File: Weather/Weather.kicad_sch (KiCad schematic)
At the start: 48 parts

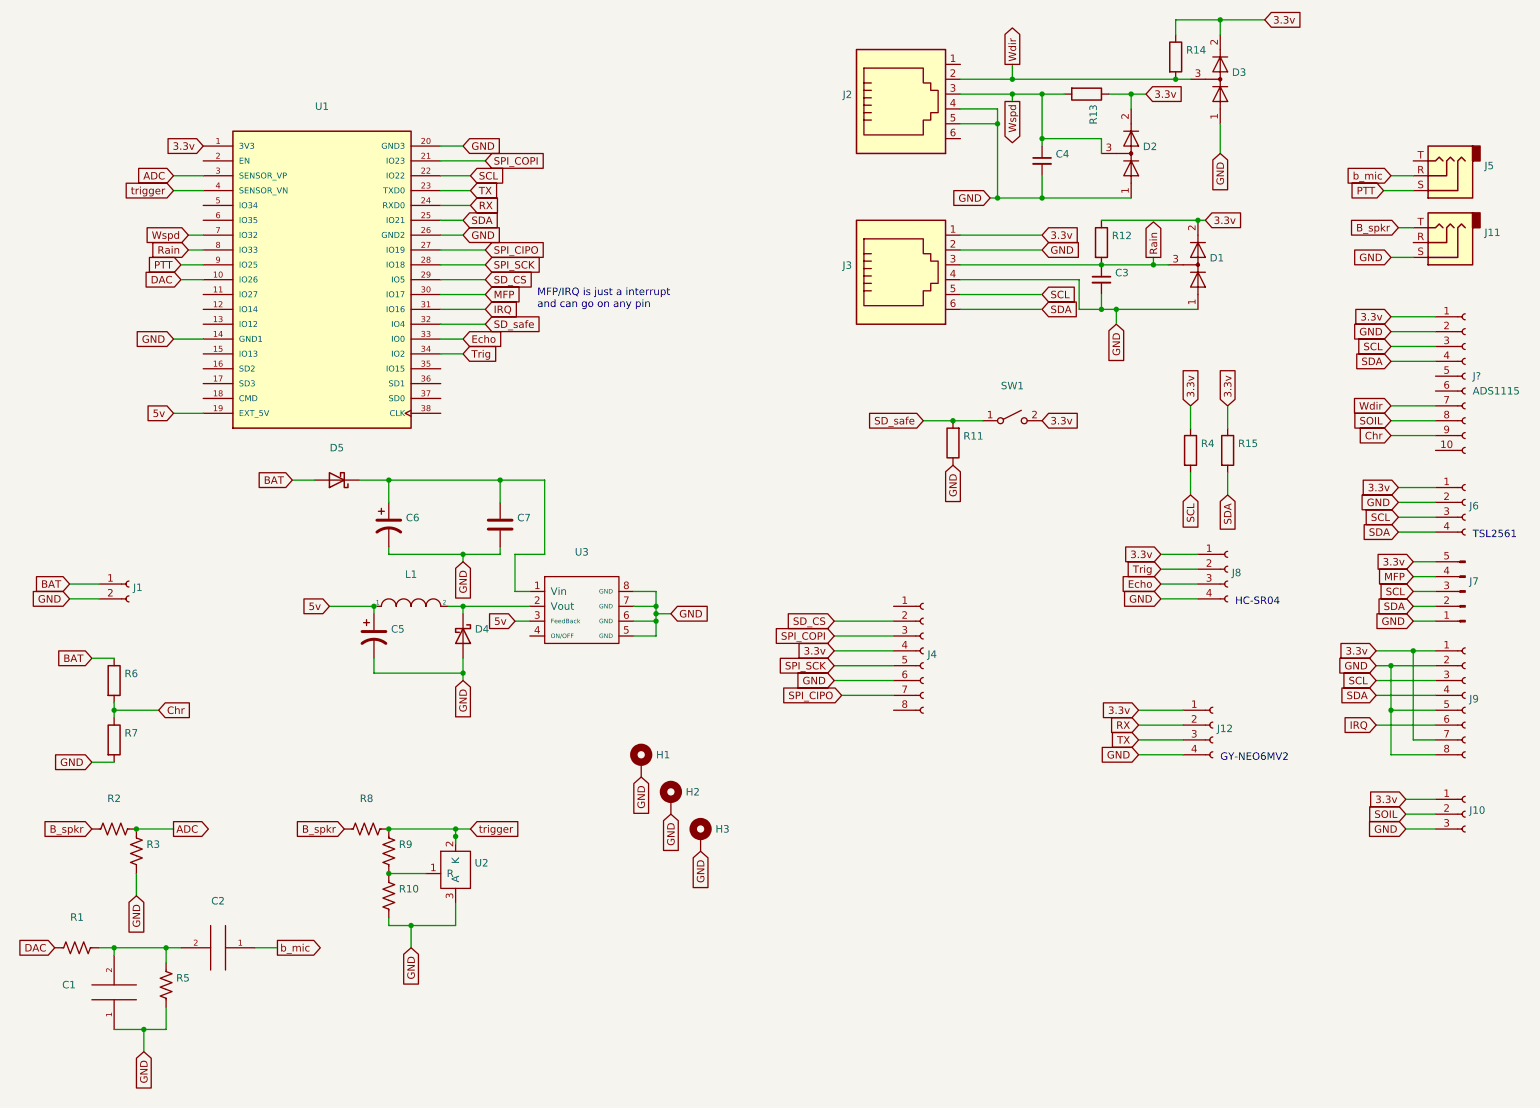
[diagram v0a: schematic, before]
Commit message: Missed some files and corrected a resistor setup
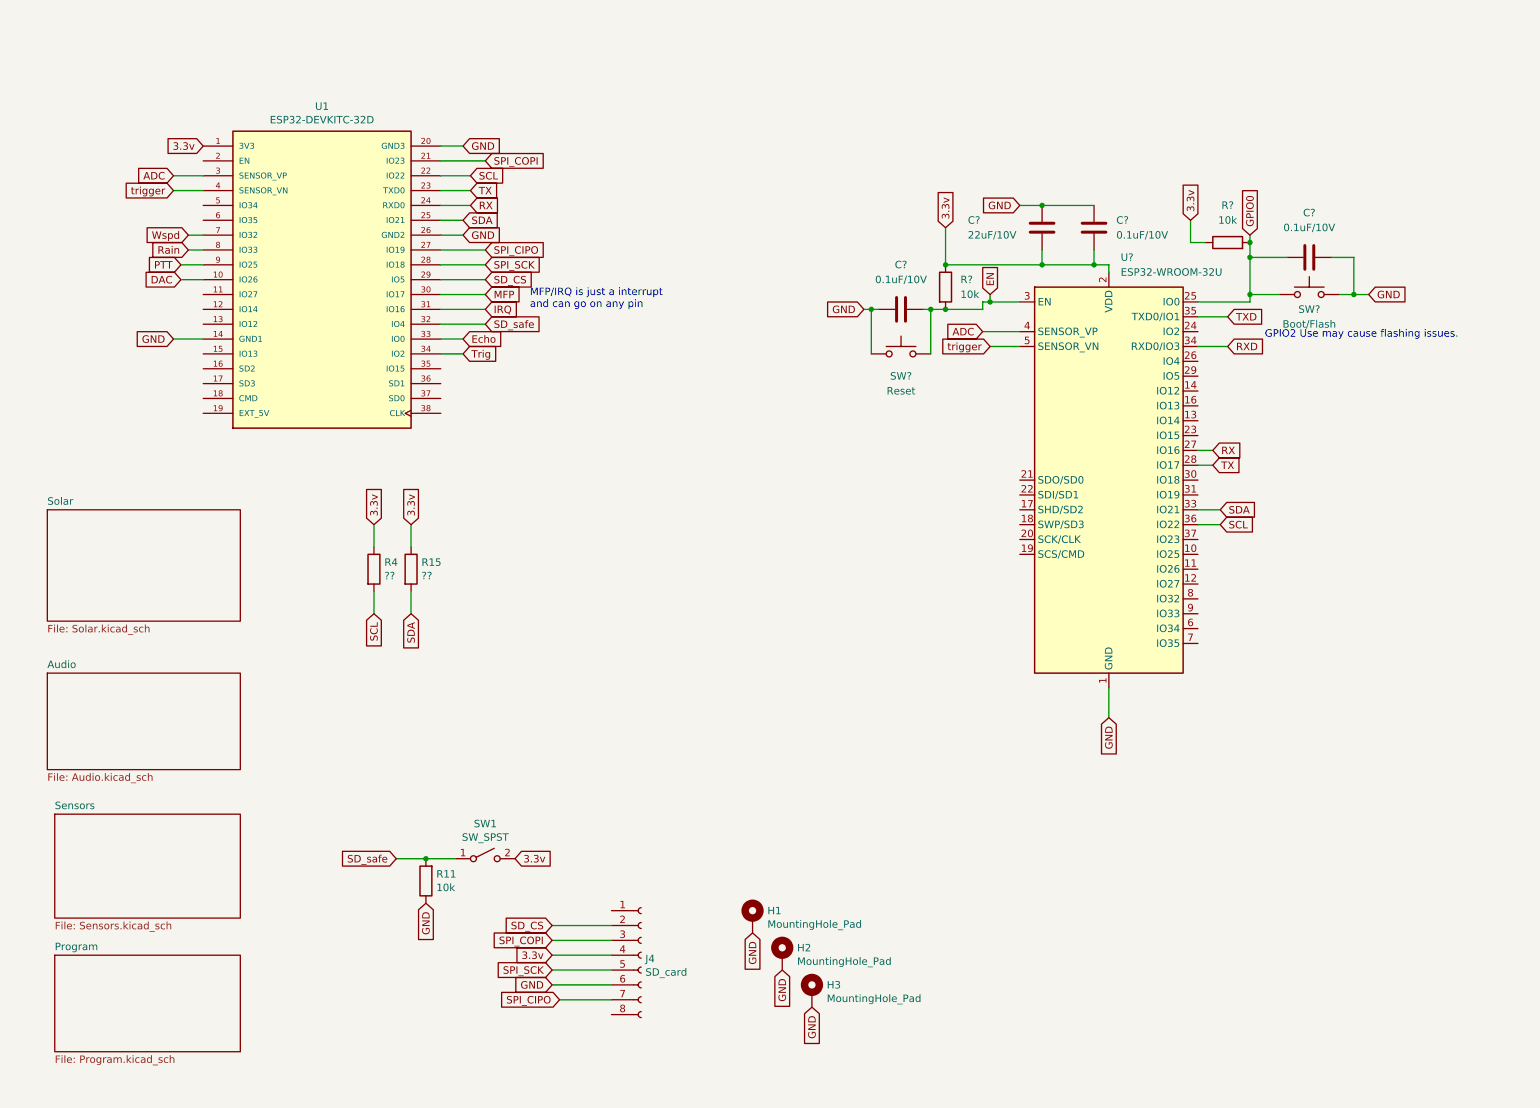
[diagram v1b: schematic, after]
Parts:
- removed C1, C2: (no value), symbol pspice:CAP
- removed C3, C4: (no value), symbol Device:C_Small
- removed C5, C6: (no value), symbol Device:CP1
- removed C7: (no value), symbol Device:C
- removed D1, D2, D3: (no value), symbol Diode:BAV99
- removed D4: (no value), symbol Diode:1N5820
- removed D5: (no value), symbol Diode:1N5819
- removed J1: (no value), symbol Connector:Conn_01x02_Female
- removed J10: (no value), symbol Connector:Conn_01x03_Female
- removed J11, J5: (no value), symbol Connector:AudioJack3
- removed J12, J6, J8: (no value), symbol Connector:Conn_01x04_Female
- removed J2, J3: (no value), symbol Connector:RJ12
- removed J7: (no value), symbol Connector:Conn_01x05_Male
- removed J9: (no value), symbol Connector:Conn_01x08_Female
- removed J?: ADS1115, symbol Connector:Conn_01x10_Female
- removed L1: (no value), symbol pspice:INDUCTOR
- removed R1, R10, R2, R3, R5, R8, R9: (no value), symbol Device:R_US
- removed R12, R13, R14, R6, R7: (no value), symbol Device:R
- removed U2: (no value), symbol Weather-rescue:CJ431
- removed U3: (no value), symbol Darty_stuff:XL1509-5.0E1
- added C? (x3): 0.1uF/10V, symbol Device:C
- added C?: 22uF/10V, symbol Device:C
- added R? (x2): 10k, symbol Device:R
- added SW?: Boot/Flash, symbol Switch:SW_Push
- added SW?: Reset, symbol Switch:SW_Push
- added U?: ESP32-WROOM-32U, RF_Module:ESP32-WROOM-32U, symbol RF_Module:ESP32-WROOM-32U
- H1, H2, H3: value (none) -> MountingHole_Pad; footprint (none) -> MountingHole:MountingHole_3.2mm_M3_Pad_Via
- J4: value (none) -> SD_card; footprint (none) -> Connector_PinSocket_2.54mm:PinSocket_1x08_P2.54mm_Vertical
- R11: value (none) -> 10k; footprint (none) -> Resistor_SMD:R_1206_3216Metric_Pad1.30x1.75mm_HandSolder
- R15, R4: value (none) -> ??; footprint (none) -> Resistor_THT:R_Axial_DIN0207_L6.3mm_D2.5mm_P7.62mm_Horizontal
- SW1: value (none) -> SW_SPST; footprint (none) -> Connector_PinHeader_2.54mm:PinHeader_1x02_P2.54mm_Vertical
- U1: value (none) -> ESP32-DEVKITC-32D; footprint (none) -> ESP32-DEVKITC-32D:MODULE_ESP32-DEVKITC-32D
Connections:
- net 3.3v: now also C?.2, C?.2, R?.1, R?.1, U?.2 (VDD)
- net ADC: now also U?.4 (SENSOR_VP)
- net GND: now also C?.1, C?.1, C?.1, C?.2, SW?.1, SW?.2, U?.1 (GND), U?.15 (GND), U?.38 (GND), U?.39 (GND)
- net RX: now also U?.27 (IO16)
- net SCL: now also U?.36 (IO22)
- net SDA: now also U?.33 (IO21)
- net TX: now also U?.28 (IO17)
- net trigger: now also U?.5 (SENSOR_VN)
- net 5v: no longer names the net of U1.19 (EXT_5V)
- new net EN: C?.1, R?.2, SW?.2, U?.3 (EN)
- new net GPIO0: C?.2, R?.2, SW?.1, U?.25 (IO0)
- new net RXD: U?.34 (RXD0/IO3)
- new net TXD: U?.35 (TXD0/IO1)
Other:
- added sheet Audio (Audio.kicad_sch)
- added sheet Program (Program.kicad_sch)
- added sheet Sensors (Sensors.kicad_sch)
- added sheet Solar (Solar.kicad_sch)
- note added: "GPIO2 Use may cause flashing issues."
- note removed: "GY-NEO6MV2"
- note removed: "HC-SR04"
- note removed: "TSL2561"
- moved on the sheet: H1, H2, H3, J4, R11, R15, R4, SW1
